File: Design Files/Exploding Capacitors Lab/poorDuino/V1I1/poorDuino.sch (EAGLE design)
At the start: 53 parts, among them T1 FDN340P, U1 NCP1117ST50T3G, U2 LP2985-33DBVR, U3 ATMEGA16U2-MU(R), U5 LMV358IDGKR, X1 POWERSUPPLY_DC21MMX, X2 USB-B_TH, Y1 16MHz, Y2 CSTCE16M0V53-R0 16MHZ

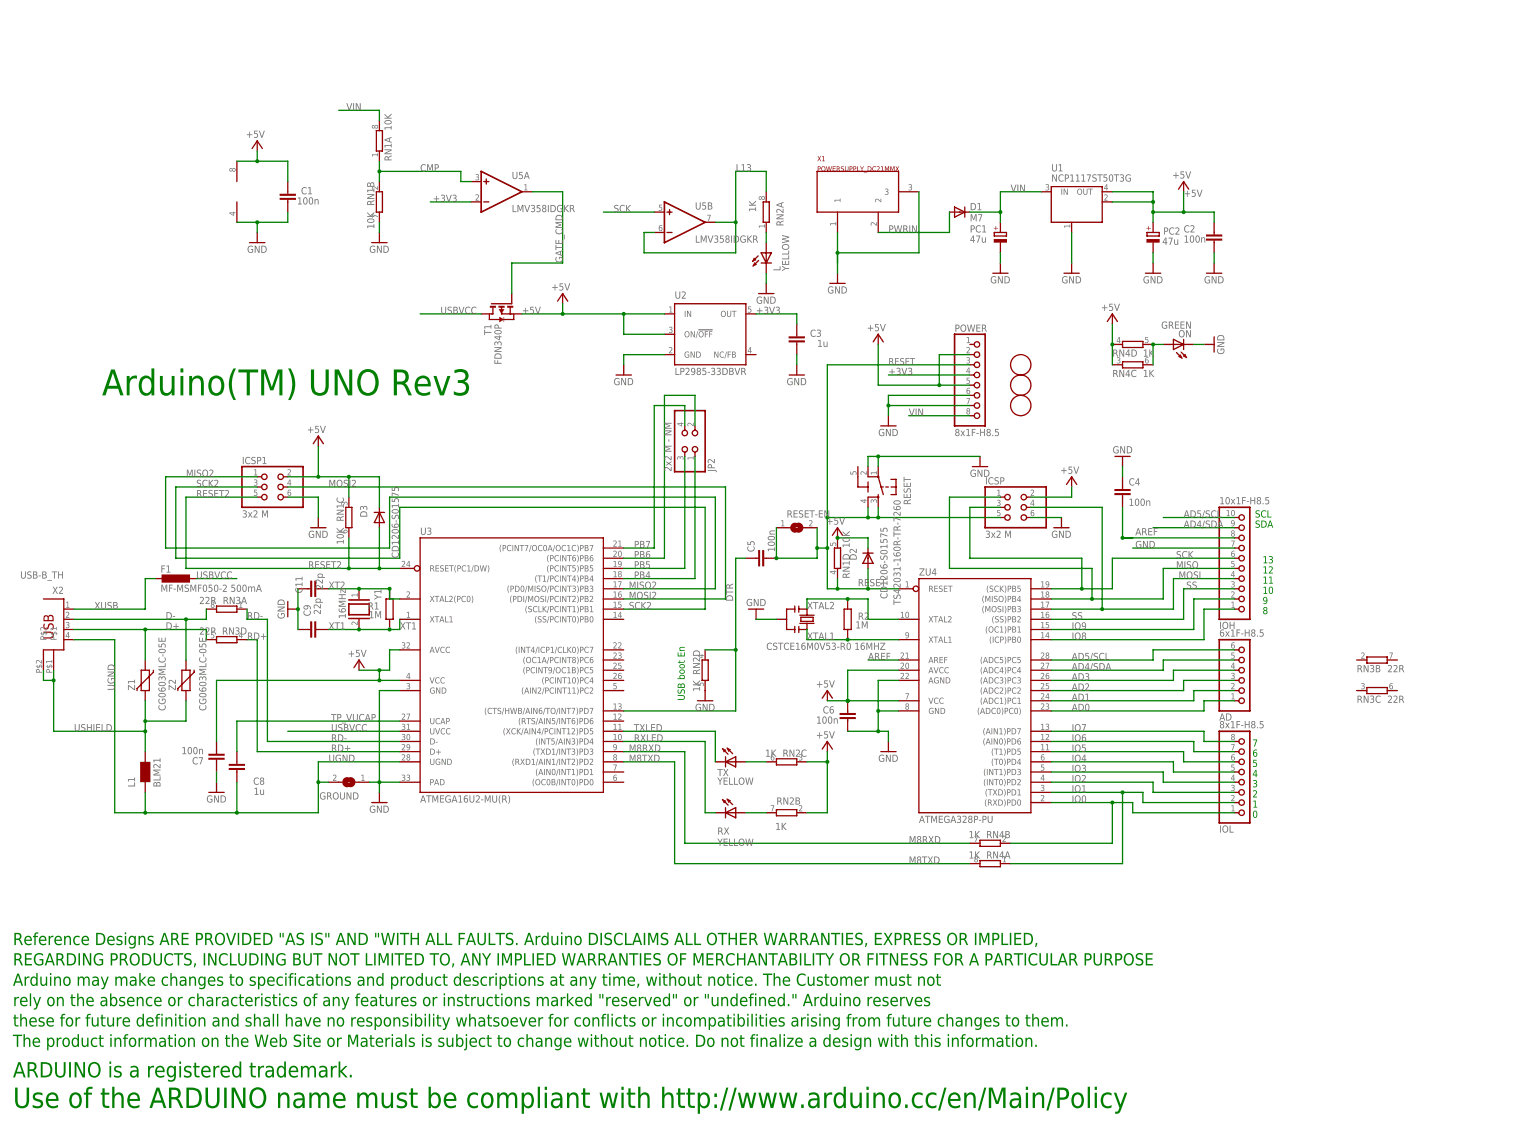
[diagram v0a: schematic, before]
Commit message: Atmega16U2 with surroundings removed
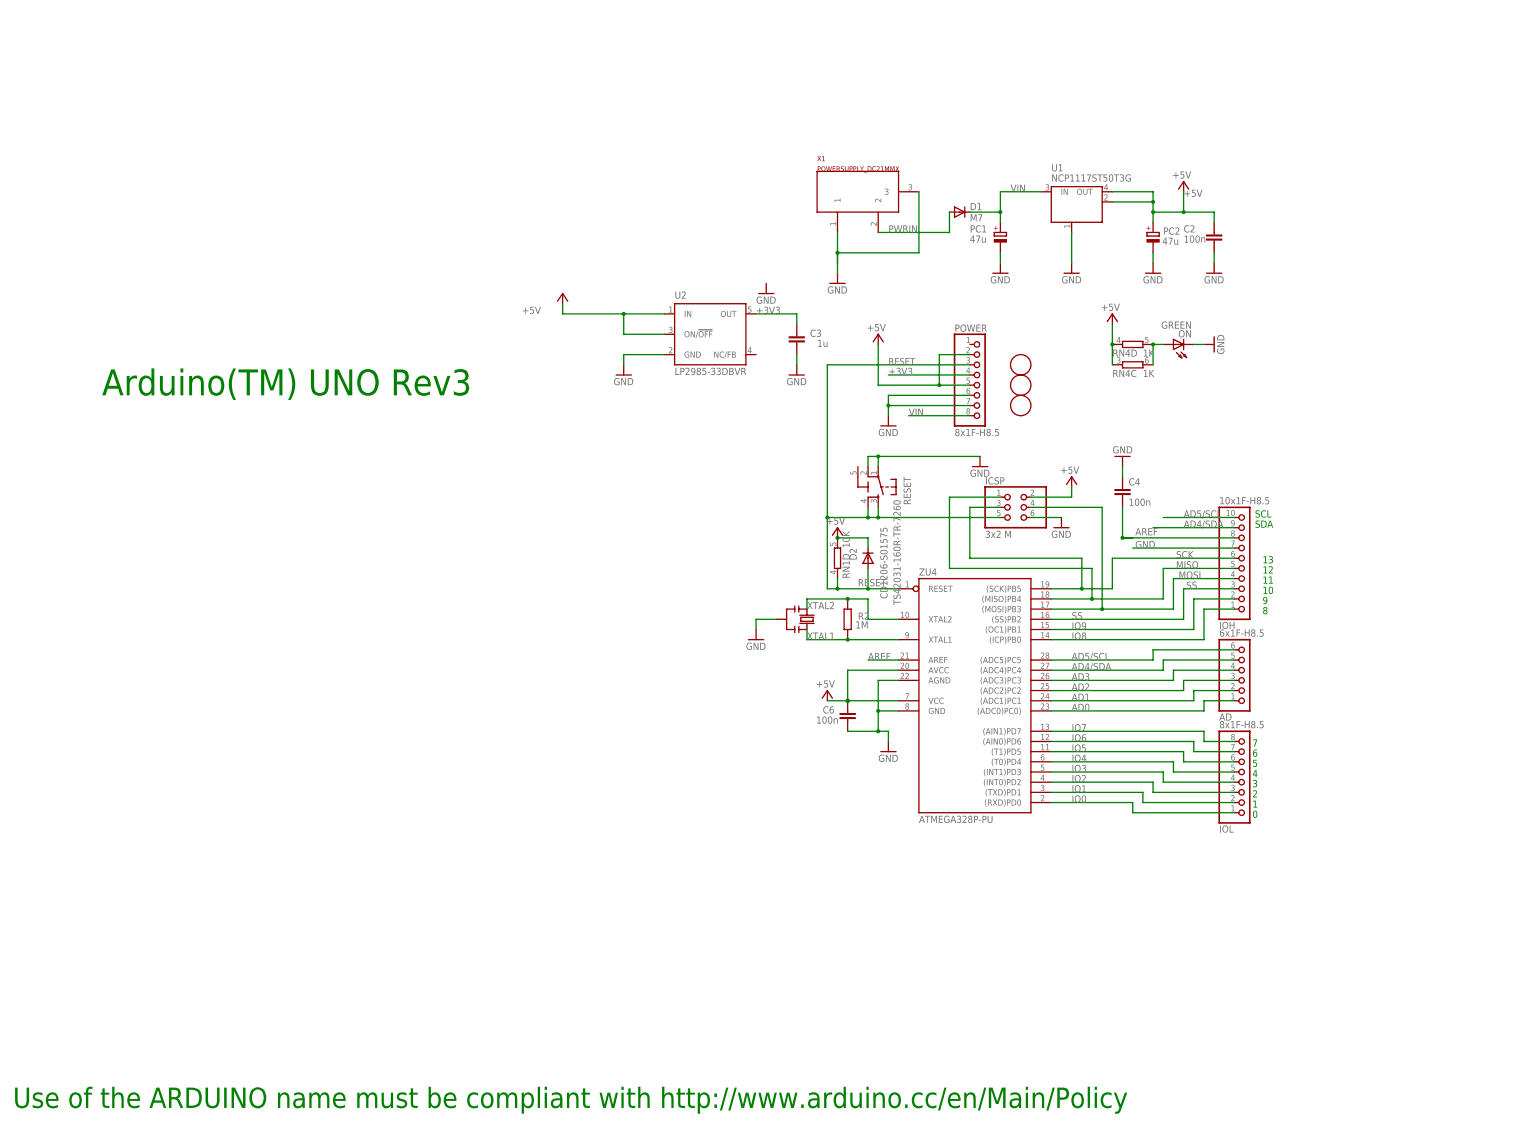
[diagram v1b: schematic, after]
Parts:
- removed C1, C5, C7: 100n, SmartPrj:C-EU0603-RND
- removed C11, C9: 22p, SmartPrj:C-EU0603-RND
- removed C8: 1u, SmartPrj:C-EU0603-RND
- removed D3: CD1206-S01575, diode:DIODE-MINIMELF
- removed F1: MF-MSMF050-2 500mA, rcl:L-EUL1812
- removed GROUND, RESET-EN: (no value), jumper:SJ
- removed ICSP1: 3x2 M, SmartPrj:PINHD-2X3
- removed JP2: 2x2 M - NM, SmartPrj:PINHD-2X2
- removed L, RX, TX: YELLOW, led:LEDCHIP-LED0805
- removed L1: BLM21, wuerth-elektronik:WE-CBF_0805
- removed R1: 1M, SmartPrj:R-EU_R0603
- removed RN2: 1K, resistor-dil:4R-NCAY16
- removed RN3: 22R, resistor-dil:4R-NCAY16
- removed T1: FDN340P, zetex:PMOSSOT23
- removed U$1: DISCLAIMER, SmartPrj:DISCLAIMER
- removed U3: ATMEGA16U2-MU(R), SmartPrj:ATMEGA16U2-MU
- removed U5: LMV358IDGKR, linear:LMV358MMX
- removed X2: USB-B_TH, SmartPrj:PN61729
- removed Y1: 16MHz, SmartPrj:XTAL/S
- removed Z1, Z2: CG0603MLC-05E, varistor:VARISTORCN0603
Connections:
- removed net CMP: RN1A.1, RN1B.1, U5A.+IN
- removed net D+: RN3D.2, X2.3, Z1.1
- removed net D-: RN3A.2, X2.2, Z2.1
- removed net DTR: C5.1, RN2D.1, U3.(CTS/HWB/AIN6/TO/INT7)PD7
- removed net GATE_CMD: T1.G, U5A.OUT
- removed net L13: RN2A.2, U5B.-IN, U5B.OUT
- removed net M8RXD: RN4B.2, U3.(TXD1/INT3)PD3
- removed net M8TXD: RN4A.2, U3.(RXD1/AIN1/INT2)PD2
- removed net MISO2: ICSP1.1, U3.(PD0/MISO/PCINT3)PB3
- removed net MOSI2: ICSP1.4, U3.(PDI/MOSI/PCINT2)PB2
- removed net N$1: L.A, RN2A.1
- removed net N$35: RN2B.2, RX.A
- removed net N$36: RN2C.2, TX.A
- removed net PB4: JP2.1, U3.(T1/PCINT4)PB4
- removed net PB5: JP2.3, U3.(PCINT5)PB5
- removed net PB6: JP2.2, U3.(PCINT6)PB6
- removed net PB7: JP2.4, U3.(PCINT7/OC0A/OC1C)PB7
- removed net RD+: RN3D.1, U3.D+
- removed net RD-: RN3A.1, U3.D-
- removed net RESET2: D3.A, ICSP1.5, RN1C.2, U3.RESET(PC1/DW)
- removed net RXLED: RX.C, U3.(INT5/AIN3)PD4
- removed net SCK2: ICSP1.3, U3.(SCLK/PCINT1)PB1
- removed net TP_VUCAP: C8.1, U3.UCAP
- removed net TXLED: TX.C, U3.(XCK/AIN4/PCINT12)PD5
- removed net UGND: C8.2, GROUND.2, L1.1, U3.UGND, X2.4
- removed net USBVCC: F1.1, T1.D, U3.UVCC
- removed net USHIELD: L1.2, X2.P$1, X2.P$2, Z1.2, Z2.2
- removed net XT1: C9.1, R1.1, U3.XTAL1, Y1.2
- removed net XT2: C11.1, R1.2, U3.XTAL2(PC0), Y1.1
- removed net XUSB: F1.2, X2.1
- net +3V3: no longer U5A.-IN
- net +5V: no longer C1.2, C7.1, D3.C, ICSP1.2, RN1C.1, RN2B.1, RN2C.1, T1.S, U3.AVCC, U3.VCC, U5P.V+
- net GND: no longer C1.1, C11.2, C7.2, C9.2, GROUND.1, ICSP1.6, L.C, RN1B.2, RN2D.2, U3.GND, U3.PAD, U5P.V-
- net IO0: no longer RN4B.1
- net IO1: no longer RN4A.1
- net RESET: no longer C5.2, RESET-EN.1, RESET-EN.2
- net SCK: no longer U5B.+IN
- net VIN: no longer RN1A.2
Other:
- note removed: "USB boot En"

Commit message: Power supply modification
LDOs, which were originaly in Arduino project, have been replaced to
LD1117xxx.  /schematic only/
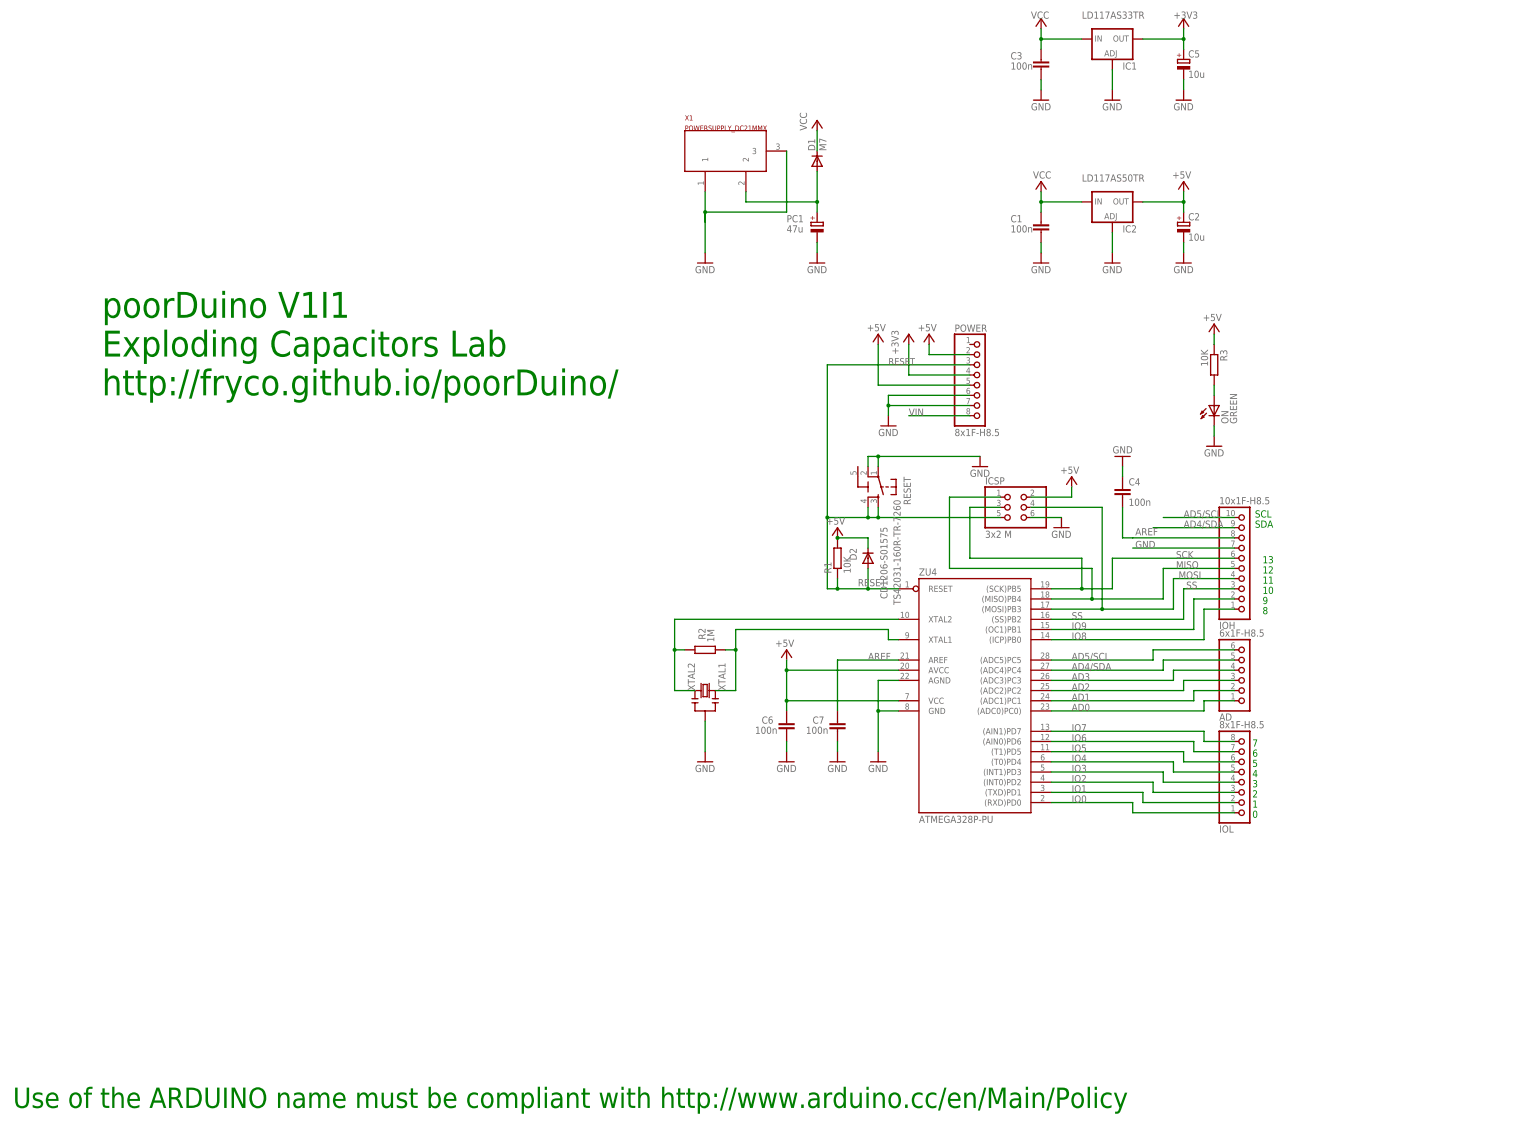
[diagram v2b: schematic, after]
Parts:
- removed FD1, FD2, FD3: FIDUCIALMOUNT, SmartPrj:FIDUCIALMOUNT
- removed PC2: 47u, rcl:CPOL-EUD
- removed RN1: 10K, resistor-dil:4R-NCAY16
- removed RN4: 1K, resistor-dil:4R-NCAY16
- removed U1: NCP1117ST50T3G, linear:MC33269ST-3.3T3
- removed U2: LP2985-33DBVR, SmartPrj:LP2985-XXDBVR33
- added C1, C7: 100n, SmartPrj:C-EUC0805
- added C5: 10u, rcl:CPOL-EUSMCA
- added IC1: LD117AS33TR, v-reg:LD117AS33TR
- added IC2: LD117AS50TR, v-reg:LD117AS50TR
- added R1, R3: 10K, SmartPrj:R-EU_R0805
- C2: value 100n -> 10u; device SmartPrj:C-EU0603-RND -> rcl:CPOL-EUSMCA
- C3: value 1u -> 100n; device SmartPrj:C-EU0603-RND -> SmartPrj:C-EUC0805
- C4, C6: device SmartPrj:C-EU0603-RND -> SmartPrj:C-EUC0805
- R2: device SmartPrj:R-EU_R0603 -> SmartPrj:R-EU_R0805
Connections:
- new net VCC: C1.2, C3.2, D1.C, IC1.IN, IC2.IN
- net +3V3: now also C5.+, IC1.OUT; no longer C3.2, U2.OUT
- net +5V: now also C2.+, IC2.OUT, R1.2, R3.1; no longer C2.2, PC2.+, RN1D.2, RN4C.1, RN4D.1, U1.OUT, U1.OUT@1, U2.IN, U2.ON/!OFF
- net AREF: now also C7.2
- net GND: now also C1.1, C2.-, C5.-, C7.1, IC1.ADJ, IC2.ADJ; no longer C2.1, PC2.-, U1.GND/ADJ, U2.GND
- net N$3: now also R3.2; no longer RN4C.2, RN4D.2
- net PWRIN: now also PC1.+
- net RESET: now also R1.1; no longer RN1D.1
- net VIN: no longer D1.C, PC1.+, U1.IN
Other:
- note added: "poorDuino V1I1 Exploding Capacitors Lab http://fryco.github.io/poorDuino/"
- note removed: "Arduino(TM) UNO Rev3"
- moved on the sheet: C3, C6, D1, ON, PC1, R2, X1

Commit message: Schematic cleanup
3V3 LED status added
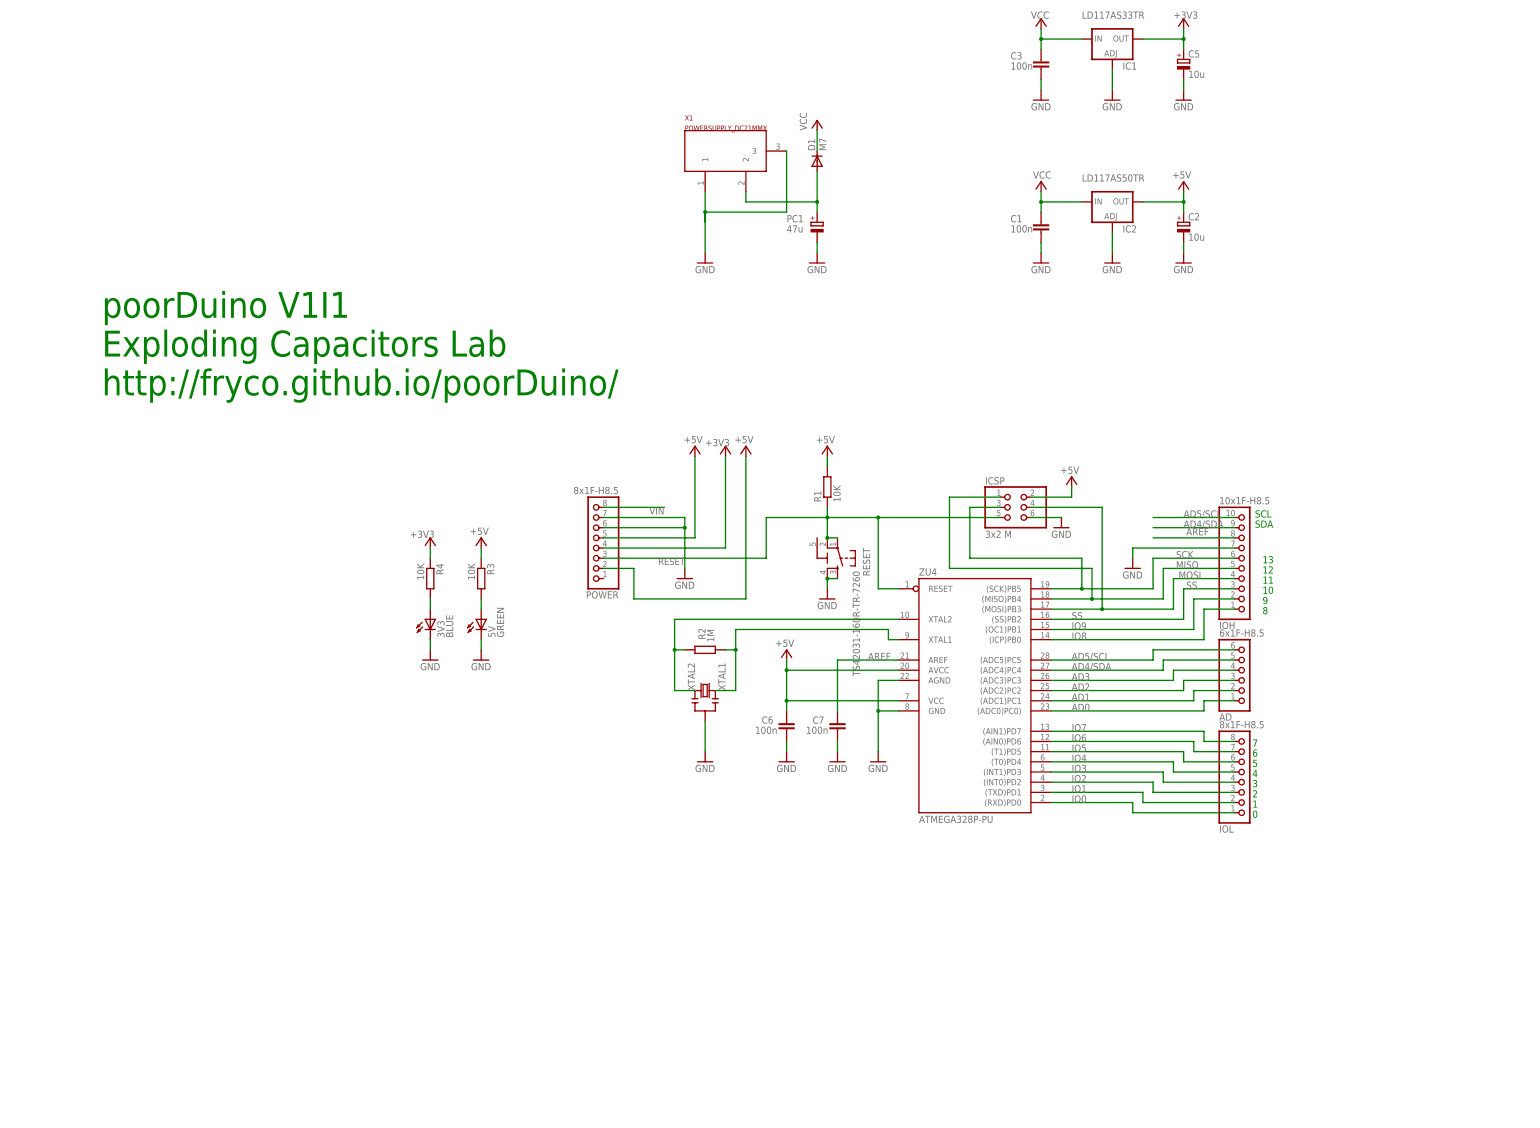
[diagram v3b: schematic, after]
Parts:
- removed C4: 100n, SmartPrj:C-EUC0805
- removed D2: CD1206-S01575, diode:DIODE-MINIMELF
- removed ON: GREEN, led:LEDCHIP-LED0805
- added 3V3: BLUE, led:LEDCHIP-LED0805
- added 5V: GREEN, led:LEDCHIP-LED0805
- added R4: 10K, SmartPrj:R-EU_R0805
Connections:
- new net N$1: 3V3.A, R4.2
- net +3V3: now also R4.1
- net +5V: no longer D2.C
- net AREF: no longer C4.2
- net GND: now also 3V3.C, 5V.C, RESET.3, RESET.4; no longer C4.1, ON.C, RESET.1, RESET.2
- net N$3: now also 5V.A; no longer ON.A
- net RESET: now also RESET.1, RESET.2; no longer D2.A, RESET.3, RESET.4
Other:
- note removed: "Use of the ARDUINO name must be compliant with http://www.arduino.cc/en/Main/Policy"
- moved on the sheet: POWER, R1, R3, RESET

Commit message: First attempt to PCB design
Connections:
- removed net VIN: POWER.8
- net VCC: now also POWER.8
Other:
- note added: "Exploding Capacitors Lab http://fryco.github.io/poorDuino/"
- note added: "V1I1"
- note removed: "poorDuino V1I1 Exploding Capacitors Lab http://fryco.github.io/poorDuino/"
- moved on the sheet: 3V3, 5V, AD, C1, C2, C3, C5, C6, C7, D1, IC1, IC2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

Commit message: PCB layout
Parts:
- added JP1: (no value), pinhead:PINHD-1X3
- added R5, R6: 4K7, SmartPrj:R-EU_R0805
- added SJ1, SJ2: (no value), jumper:SJ
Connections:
- new net N$6: R5.1, SJ1.1
- new net N$7: R6.1, SJ2.1
- new net V+: C6.2, ICSP.2, JP1.2, POWER.2, R1.2, R5.2, R6.2, ZU4.AVCC, ZU4.VCC
- net +3V3: now also JP1.3
- net +5V: now also JP1.1; no longer C6.2, ICSP.2, POWER.2, R1.2, ZU4.AVCC, ZU4.VCC
- net AD4/SDA: now also SJ2.2
- net AD5/SCL: now also SJ1.2
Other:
- moved on the sheet: 3V3, 5V, AD, C1, C2, C3, C5, C6, C7, IC1, IC2, ICSP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
